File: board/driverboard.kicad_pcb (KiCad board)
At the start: 2 copper layers, 49.5 x 54.6 mm, 39 parts, among them J1 RJ45, J2 RJ45, P1 HE10-10, Q1 NDS355, Q2 NDS355, Q3 NDS355, Q4 NDS355, Q5 NDS355, Q6 NDS355, Q7 NDS355, Q8 NDS355, U1 74HC595, U2 TS2937

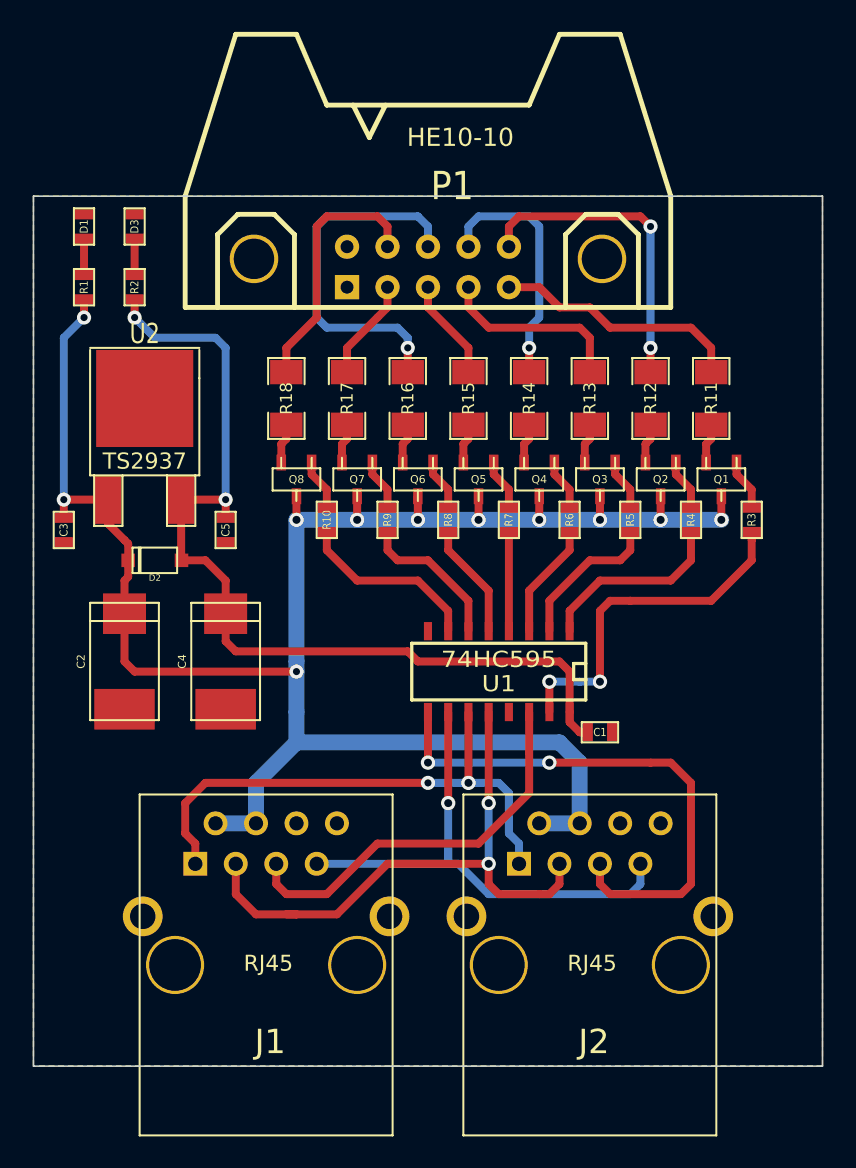
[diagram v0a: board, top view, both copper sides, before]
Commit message: Cleaned up silkscreen
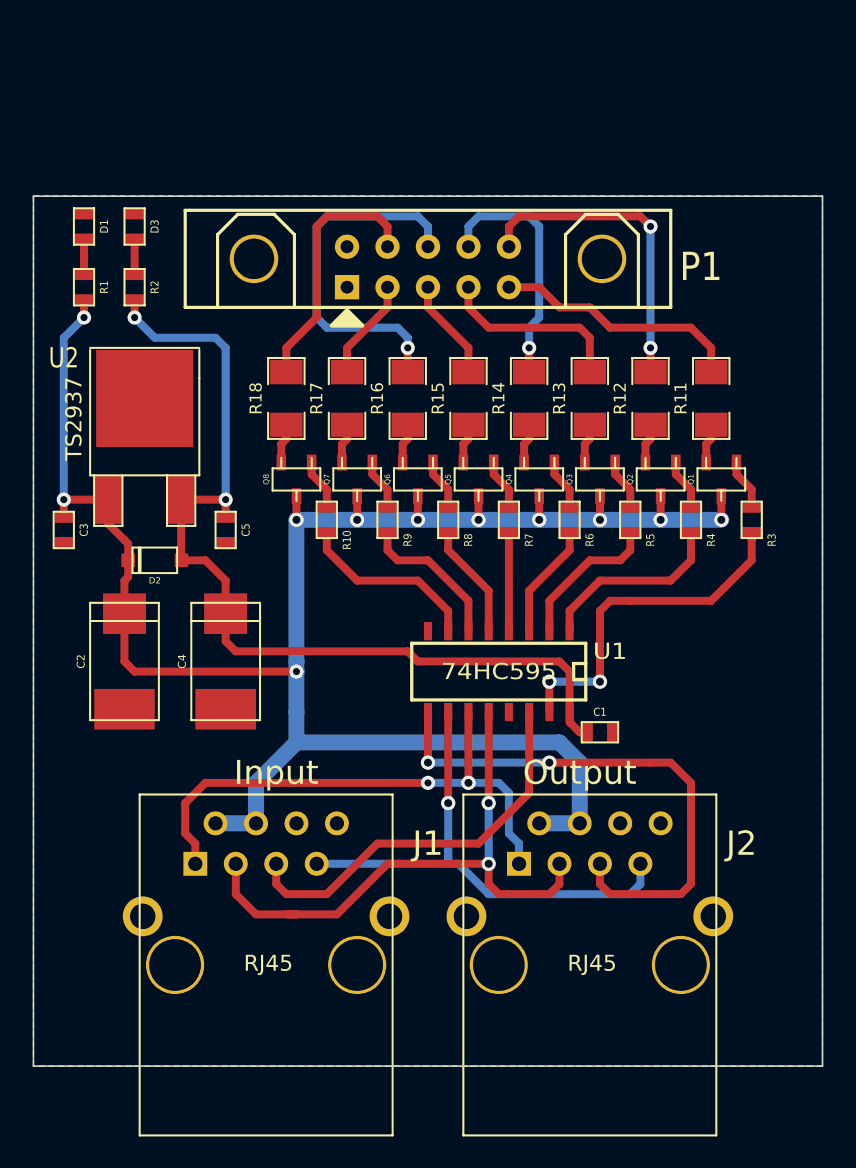
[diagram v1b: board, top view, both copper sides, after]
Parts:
- added G***: logo_silkbot_30_00mm, logo_silkbot_30_00mm, B.Cu at (129.5, 48.1)
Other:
- board text added: "7 segment led display driver"
- board text added: "Input"
- board text added: "Output"
- board text added: "Sebastian Schumb 2014"
- board text added: "Version 1.0"
- board text added: "https://github.com/LongHairedHacker/HetpaLED"

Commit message: Added holes to driver board
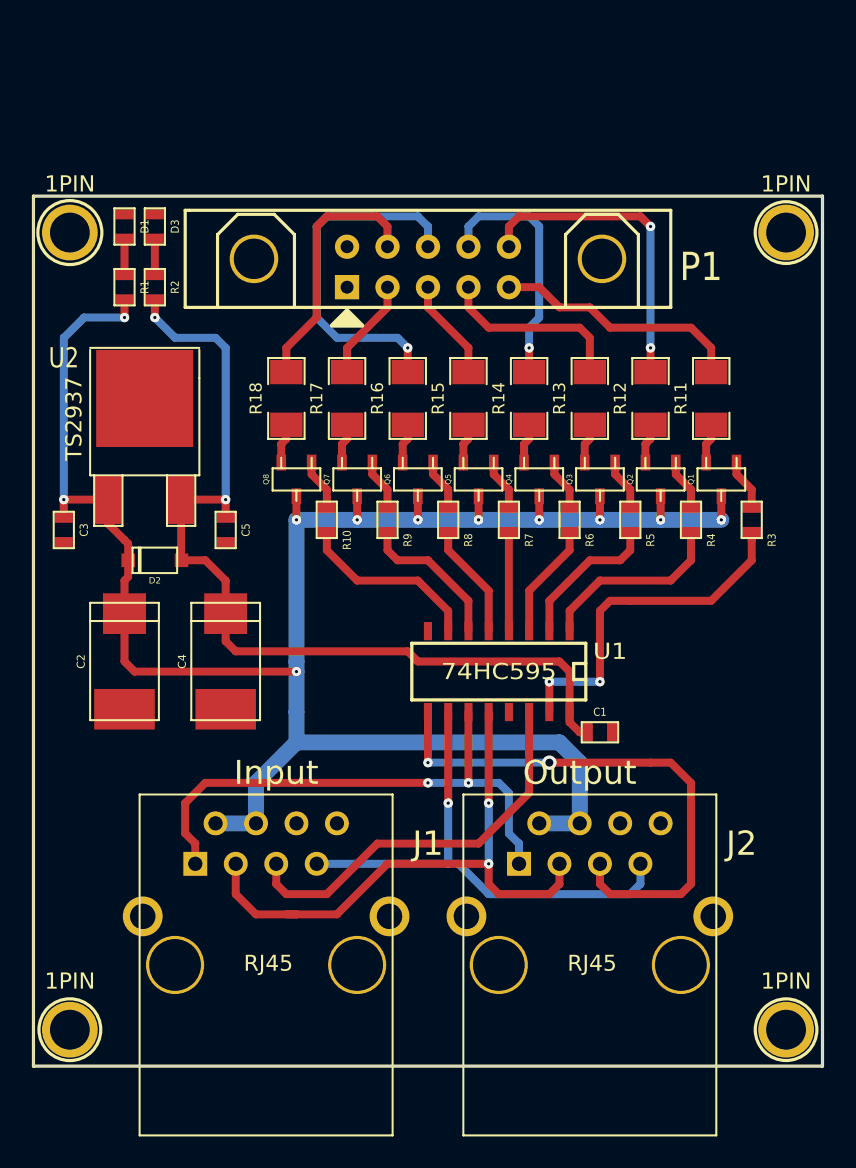
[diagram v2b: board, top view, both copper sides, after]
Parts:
- added 1PIN: P***, 1pin, F.Cu at (102.0, 36.6)
- added 1PIN: P***, 1pin, F.Cu at (102.0, 86.6)
- added 1PIN: P***, 1pin, F.Cu at (146.9, 86.6)
- added 1PIN: P***, 1pin, F.Cu at (146.9, 36.6)
- moved D1 2.54 mm to (105.4, 36.2)
- moved R1 2.54 mm to (105.4, 40.0)
- moved D3 1.27 mm to (107.3, 36.2)
- moved R2 1.27 mm to (107.3, 40.0)
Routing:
- net +24V: track 124.7 -> 127.2 mm
- net +5V: track 59.0 -> 57.7 mm
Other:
- rule via_min_drill: 0.508 -> 0.1524
- rule via_min_size: 0.889 -> 0.508
